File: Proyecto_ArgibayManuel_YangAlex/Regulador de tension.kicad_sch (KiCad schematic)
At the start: 11 parts, among them IC1 LM1117

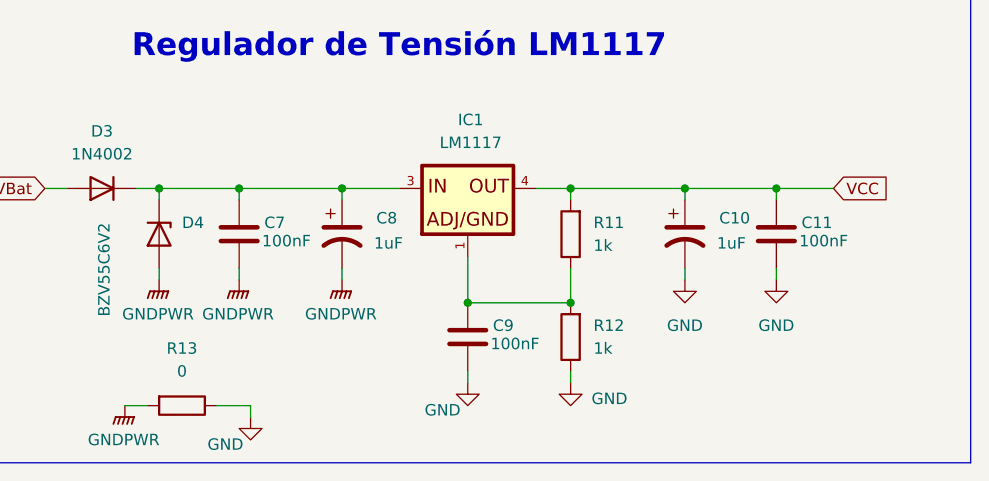
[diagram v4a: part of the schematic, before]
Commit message: Empiezo layout, cambio footprints y arreglo esquematico
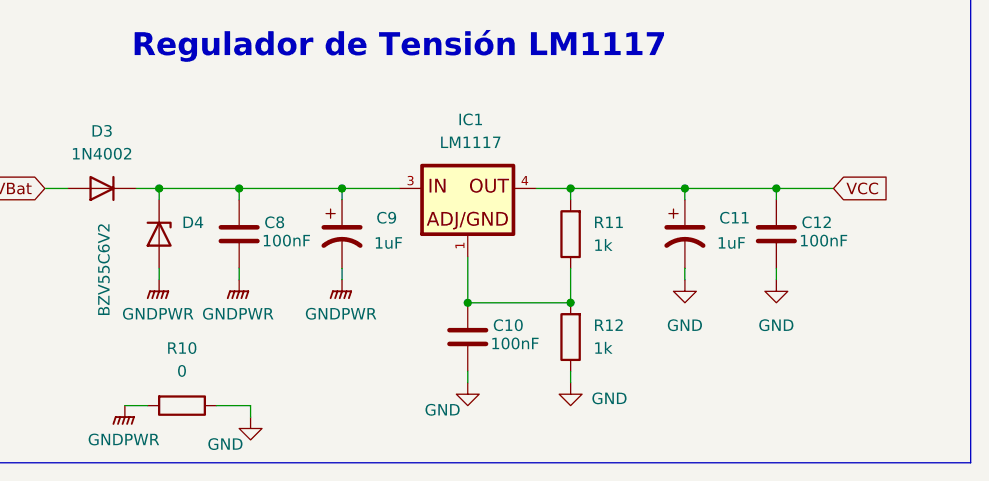
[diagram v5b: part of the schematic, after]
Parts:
- C10: renamed from C9; footprint Capacitor_SMD:C_0805_2012Metric -> Capacitor_THT:CP_Radial_D5.0mm_P2.00mm
- C11: renamed from C10; footprint Capacitor_SMD:C_0805_2012Metric -> Capacitor_THT:CP_Radial_D5.0mm_P2.00mm
- C12: renamed from C11; footprint Capacitor_SMD:C_0805_2012Metric -> Capacitor_THT:CP_Radial_D5.0mm_P2.00mm
- C8: renamed from C7; footprint Capacitor_SMD:C_0805_2012Metric -> Capacitor_THT:CP_Radial_D5.0mm_P2.00mm
- C9: renamed from C8; footprint Capacitor_SMD:C_0805_2012Metric -> Capacitor_THT:CP_Radial_D5.0mm_P2.00mm
- IC1: footprint LM1117:SOT223 -> Footprints:LM1117
- R10: renamed from R13; footprint Resistor_THT:R_Axial_DIN0204_L3.6mm_D1.6mm_P1.90mm_Vertical -> Resistor_SMD:R_0805_2012Metric
- R11, R12: footprint Resistor_THT:R_Axial_DIN0204_L3.6mm_D1.6mm_P1.90mm_Vertical -> Resistor_SMD:R_0805_2012Metric
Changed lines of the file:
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@@
 		(on_board yes)
 		(dnp no)
-		(property "Reference" "#PWR039"
+		(property "Reference" "#PWR027"
 			(at 138.43 106.68 0)
 			(effects
@@
 			(project "Proyecto_ArgibayManuel_YangAlex"
 				(path "/b2dde924-33f5-41ab-a1bf-811873450a89/586cebd2-39d7-435a-989d-0b17f5522a13"
-					(reference "#PWR039")
+					(reference "#PWR027")
 					(unit 1)
 				)
@@
 		(dnp no)
 		(fields_autoplaced yes)
-		(property "Reference" "#PWR025"
+		(property "Reference" "#PWR026"
 			(at 137.16 90.17 0)
 			(effects
@@
 			(project "Proyecto_ArgibayManuel_YangAlex"
 				(path "/b2dde924-33f5-41ab-a1bf-811873450a89/586cebd2-39d7-435a-989d-0b17f5522a13"
-					(reference "#PWR025")
+					(reference "#PWR026")
 					(unit 1)
 				)
@@
 		(dnp no)
 		(fields_autoplaced yes)
-		(property "Reference" "#PWR029"
+		(property "Reference" "#PWR031"
 			(at 186.69 91.44 0)
 			(effects
@@
 			(project "Proyecto_ArgibayManuel_YangAlex"
 				(path "/b2dde924-33f5-41ab-a1bf-811873450a89/586cebd2-39d7-435a-989d-0b17f5522a13"
-					(reference "#PWR029")
+					(reference "#PWR031")
 					(unit 1)
 				)
@@
 			)
 		)
-		(property "Footprint" "LM1117:SOT223"
+		(property "Footprint" "Footprints:LM1117"
 			(at 162.56 74.93 0)
 			(effects
@@
 		(on_board yes)
 		(dnp no)
-		(property "Reference" "C7"
+		(property "Reference" "C8"
 			(at 139.954 78.74 0)
 			(effects
@@
 			)
 		)
-		(property "Footprint" "Capacitor_SMD:C_0805_2012Metric"
+		(property "Footprint" "Capacitor_THT:CP_Radial_D5.0mm_P2.00mm"
 			(at 138.1252 83.82 0)
 			(effects
@@
 			(project "Proyecto_ArgibayManuel_YangAlex"
 				(path "/b2dde924-33f5-41ab-a1bf-811873450a89/586cebd2-39d7-435a-989d-0b17f5522a13"
-					(reference "C7")
+					(reference "C8")
 					(unit 1)
 				)
@@
 		(on_board yes)
 		(dnp no)
-		(property "Reference" "#PWR028"
+		(property "Reference" "#PWR030"
 			(at 173.99 102.87 0)
 			(effects
@@
 			(project "Proyecto_ArgibayManuel_YangAlex"
 				(path "/b2dde924-33f5-41ab-a1bf-811873450a89/586cebd2-39d7-435a-989d-0b17f5522a13"
-					(reference "#PWR028")
+					(reference "#PWR030")
 					(unit 1)
 				)
@@
 		(dnp no)
 		(fields_autoplaced yes)
-		(property "Reference" "R13"
+		(property "Reference" "R10"
 			(at 130.81 92.71 90)
 			(effects
@@
 			)
 		)
-		(property "Footprint" "Resistor_THT:R_Axial_DIN0204_L3.6mm_D1.6mm_P1.90mm_Vertical"
+		(property "Footprint" "Resistor_SMD:R_0805_2012Metric"
 			(at 130.81 97.282 90)
 			(effects
@@
 			(project "Proyecto_ArgibayManuel_YangAlex"
 				(path "/b2dde924-33f5-41ab-a1bf-811873450a89/586cebd2-39d7-435a-989d-0b17f5522a13"
-					(reference "R13")
+					(reference "R10")
 					(unit 1)
 				)
@@
 		(on_board yes)
 		(dnp no)
-		(property "Reference" "C8"
+		(property "Reference" "C9"
 			(at 152.4 78.232 0)
 			(effects
@@
 			)
 		)
-		(property "Footprint" "Capacitor_SMD:C_0805_2012Metric"
+		(property "Footprint" "Capacitor_THT:CP_Radial_D5.0mm_P2.00mm"
 			(at 148.59 80.01 0)
 			(effects
@@
 			(project "Proyecto_ArgibayManuel_YangAlex"
 				(path "/b2dde924-33f5-41ab-a1bf-811873450a89/586cebd2-39d7-435a-989d-0b17f5522a13"
-					(reference "C8")
+					(reference "C9")
 					(unit 1)
 				)
@@
 		(dnp no)
 		(fields_autoplaced yes)
-		(property "Reference" "#PWR024"
+		(property "Reference" "#PWR025"
 			(at 128.27 90.17 0)
 			(effects
@@
 			(project "Proyecto_ArgibayManuel_YangAlex"
 				(path "/b2dde924-33f5-41ab-a1bf-811873450a89/586cebd2-39d7-435a-989d-0b17f5522a13"
-					(reference "#PWR024")
+					(reference "#PWR025")
 					(unit 1)
 				)
@@
 		(dnp no)
 		(fields_autoplaced yes)
-		(property "Reference" "#PWR030"
+		(property "Reference" "#PWR032"
 			(at 196.85 91.44 0)
 			(effects
@@
 			(project "Proyecto_ArgibayManuel_YangAlex"
 				(path "/b2dde924-33f5-41ab-a1bf-811873450a89/586cebd2-39d7-435a-989d-0b17f5522a13"
-					(reference "#PWR030")
+					(reference "#PWR032")
 					(unit 1)
 				)
@@
 			)
 		)
-		(property "Footprint" "Resistor_THT:R_Axial_DIN0204_L3.6mm_D1.6mm_P1.90mm_Vertical"
+		(property "Footprint" "Resistor_SMD:R_0805_2012Metric"
 			(at 175.768 80.01 90)
 			(effects
@@
 		(dnp no)
 		(fields_autoplaced yes)
-		(property "Reference" "#PWR026"
+		(property "Reference" "#PWR028"
 			(at 148.59 90.17 0)
 			(effects
@@
 			(project "Proyecto_ArgibayManuel_YangAlex"
 				(path "/b2dde924-33f5-41ab-a1bf-811873450a89/586cebd2-39d7-435a-989d-0b17f5522a13"
-					(reference "#PWR026")
+					(reference "#PWR028")
 					(unit 1)
 				)
@@
 			)
 		)
-		(property "Footprint" "Resistor_THT:R_Axial_DIN0204_L3.6mm_D1.6mm_P1.90mm_Vertical"
+		(property "Footprint" "Resistor_SMD:R_0805_2012Metric"
 			(at 175.768 91.44 90)
 			(effects
@@
 		(on_board yes)
 		(dnp no)
-		(property "Reference" "C9"
+		(property "Reference" "C10"
 			(at 165.354 90.17 0)
 			(effects
@@
 			)
 		)
-		(property "Footprint" "Capacitor_SMD:C_0805_2012Metric"
+		(property "Footprint" "Capacitor_THT:CP_Radial_D5.0mm_P2.00mm"
 			(at 163.5252 95.25 0)
 			(effects
@@
 			(project "Proyecto_ArgibayManuel_YangAlex"
 				(path "/b2dde924-33f5-41ab-a1bf-811873450a89/586cebd2-39d7-435a-989d-0b17f5522a13"
-					(reference "C9")
+					(reference "C10")
 					(unit 1)
 				)
@@
 		(dnp no)
 		(fields_autoplaced yes)
-		(property "Reference" "#PWR038"
+		(property "Reference" "#PWR024"
 			(at 124.46 104.14 0)
 			(effects
@@
 			(project "Proyecto_ArgibayManuel_YangAlex"
 				(path "/b2dde924-33f5-41ab-a1bf-811873450a89/586cebd2-39d7-435a-989d-0b17f5522a13"
-					(reference "#PWR038")
+					(reference "#PWR024")
 					(unit 1)
 				)
@@
 		(on_board yes)
 		(dnp no)
-		(property "Reference" "#PWR027"
+		(property "Reference" "#PWR029"
 			(at 162.56 102.87 0)
 			(effects
@@
 			(project "Proyecto_ArgibayManuel_YangAlex"
 				(path "/b2dde924-33f5-41ab-a1bf-811873450a89/586cebd2-39d7-435a-989d-0b17f5522a13"
-					(reference "#PWR027")
+					(reference "#PWR029")
 					(unit 1)
 				)
@@
 		(on_board yes)
 		(dnp no)
-		(property "Reference" "C11"
+		(property "Reference" "C12"
 			(at 199.644 78.74 0)
 			(effects
@@
 			)
 		)
-		(property "Footprint" "Capacitor_SMD:C_0805_2012Metric"
+		(property "Footprint" "Capacitor_THT:CP_Radial_D5.0mm_P2.00mm"
 			(at 197.8152 83.82 0)
 			(effects
@@
 			(project "Proyecto_ArgibayManuel_YangAlex"
 				(path "/b2dde924-33f5-41ab-a1bf-811873450a89/586cebd2-39d7-435a-989d-0b17f5522a13"
-					(reference "C11")
+					(reference "C12")
 					(unit 1)
 				)
@@
 		(on_board yes)
 		(dnp no)
-		(property "Reference" "C10"
+		(property "Reference" "C11"
 			(at 190.5 78.232 0)
 			(effects
@@
 			)
 		)
-		(property "Footprint" "Capacitor_SMD:C_0805_2012Metric"
+		(property "Footprint" "Capacitor_THT:CP_Radial_D5.0mm_P2.00mm"
 			(at 186.69 80.01 0)
 			(effects
@@
 			(project "Proyecto_ArgibayManuel_YangAlex"
 				(path "/b2dde924-33f5-41ab-a1bf-811873450a89/586cebd2-39d7-435a-989d-0b17f5522a13"
-					(reference "C10")
-					(unit 1)
-				)
+					(reference "C11")
+					(unit 1)
+				)

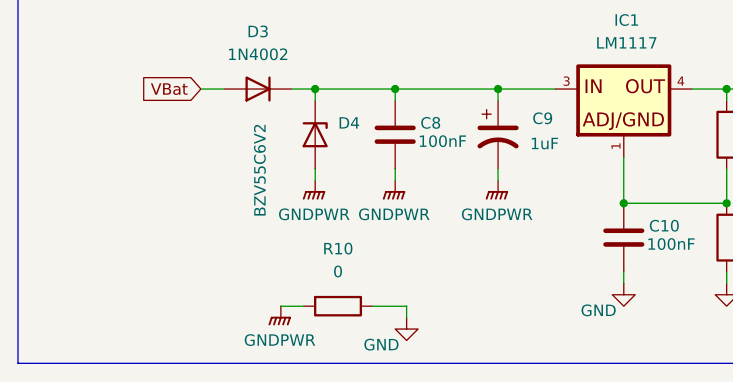
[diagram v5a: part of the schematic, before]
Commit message: Cambio de presentacion(esquematico,consumo,layout), minimas correciones en el esquematico
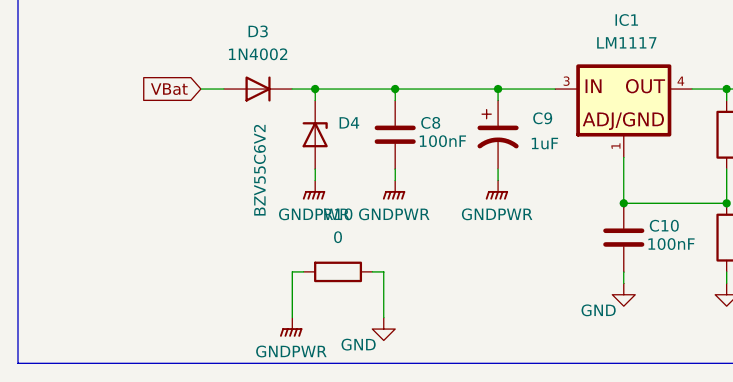
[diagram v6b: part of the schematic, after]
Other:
- moved on the sheet: R10
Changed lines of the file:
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@@
 	(wire
 		(pts
-			(xy 134.62 99.06) (xy 138.43 99.06)
+			(xy 134.62 95.25) (xy 135.89 95.25)
 		)
 		(stroke
@@
 	(wire
 		(pts
-			(xy 138.43 99.06) (xy 138.43 100.33)
+			(xy 135.89 95.25) (xy 135.89 100.33)
 		)
 		(stroke
@@
 	(wire
 		(pts
-			(xy 124.46 99.06) (xy 127 99.06)
+			(xy 125.73 95.25) (xy 127 95.25)
 		)
 		(stroke
@@
 		(pts
 			(xy 137.16 74.93) (xy 137.16 76.2)
+		)
+		(stroke
+			(width 0)
+			(type default)
+		)
+	)
+	(wire
+		(pts
+			(xy 125.73 95.25) (xy 125.73 100.33)
 		)
 		(stroke
@@
 	(symbol
 		(lib_id "power:GND")
-		(at 138.43 100.33 0)
-		(unit 1)
-		(exclude_from_sim no)
-		(in_bom yes)
-		(on_board yes)
-		(dnp no)
-		(property "Reference" "#PWR027"
-			(at 138.43 106.68 0)
+		(at 135.89 100.33 0)
+		(unit 1)
+		(exclude_from_sim no)
+		(in_bom yes)
+		(on_board yes)
+		(dnp no)
+		(property "Reference" "#PWR028"
+			(at 135.89 106.68 0)
 			(effects
 				(font
@@
 		)
 		(property "Value" "GND"
-			(at 135.636 103.378 0)
+			(at 133.096 103.378 0)
 			(effects
 				(font
@@
 		)
 		(property "Footprint" ""
-			(at 138.43 100.33 0)
+			(at 135.89 100.33 0)
 			(effects
 				(font
@@
 		)
 		(property "Datasheet" ""
-			(at 138.43 100.33 0)
+			(at 135.89 100.33 0)
 			(effects
 				(font
@@
 		)
 		(property "Description" "Power symbol creates a global label with name \"GND\" , ground"
-			(at 138.43 100.33 0)
-			(effects
-				(font
-					(size 1.27 1.27)
-				)
-				(hide yes)
-			)
-		)
-		(pin "1"
-		)
-		(instances
-			(project "Proyecto_ArgibayManuel_YangAlex"
-				(path "/b2dde924-33f5-41ab-a1bf-811873450a89/586cebd2-39d7-435a-989d-0b17f5522a13"
-					(reference "#PWR027")
+			(at 135.89 100.33 0)
+			(effects
+				(font
+					(size 1.27 1.27)
+				)
+				(hide yes)
+			)
+		)
+		(pin "1"
+		)
+		(instances
+			(project "Proyecto_ArgibayManuel_YangAlex"
+				(path "/b2dde924-33f5-41ab-a1bf-811873450a89/586cebd2-39d7-435a-989d-0b17f5522a13"
+					(reference "#PWR028")
 					(unit 1)
 				)
@@
 		(dnp no)
 		(fields_autoplaced yes)
-		(property "Reference" "#PWR026"
+		(property "Reference" "#PWR027"
 			(at 137.16 90.17 0)
 			(effects
@@
 			(project "Proyecto_ArgibayManuel_YangAlex"
 				(path "/b2dde924-33f5-41ab-a1bf-811873450a89/586cebd2-39d7-435a-989d-0b17f5522a13"
-					(reference "#PWR026")
+					(reference "#PWR027")
 					(unit 1)
 				)
@@
 		(dnp no)
 		(fields_autoplaced yes)
-		(property "Reference" "#PWR031"
+		(property "Reference" "#PWR032"
 			(at 186.69 91.44 0)
 			(effects
@@
 			(project "Proyecto_ArgibayManuel_YangAlex"
 				(path "/b2dde924-33f5-41ab-a1bf-811873450a89/586cebd2-39d7-435a-989d-0b17f5522a13"
-					(reference "#PWR031")
+					(reference "#PWR032")
 					(unit 1)
 				)
@@
 		(on_board yes)
 		(dnp no)
-		(property "Reference" "#PWR030"
+		(property "Reference" "#PWR031"
 			(at 173.99 102.87 0)
 			(effects
@@
 			(project "Proyecto_ArgibayManuel_YangAlex"
 				(path "/b2dde924-33f5-41ab-a1bf-811873450a89/586cebd2-39d7-435a-989d-0b17f5522a13"
-					(reference "#PWR030")
+					(reference "#PWR031")
 					(unit 1)
 				)
@@
 	(symbol
 		(lib_id "Device:R")
-		(at 130.81 99.06 270)
+		(at 130.81 95.25 270)
 		(unit 1)
 		(exclude_from_sim no)
@@
 		(fields_autoplaced yes)
 		(property "Reference" "R10"
-			(at 130.81 92.71 90)
+			(at 130.81 88.9 90)
 			(effects
 				(font
@@
 		)
 		(property "Value" "0"
-			(at 130.81 95.25 90)
+			(at 130.81 91.44 90)
 			(effects
 				(font
@@
 		)
 		(property "Footprint" "Resistor_SMD:R_0805_2012Metric"
-			(at 130.81 97.282 90)
+			(at 130.81 93.472 90)
 			(effects
 				(font
@@
 		)
 		(property "Datasheet" "~"
-			(at 130.81 99.06 0)
+			(at 130.81 95.25 0)
 			(effects
 				(font
@@
 		)
 		(property "Description" "Resistor"
-			(at 130.81 99.06 0)
+			(at 130.81 95.25 0)
 			(effects
 				(font
@@
 		(dnp no)
 		(fields_autoplaced yes)
-		(property "Reference" "#PWR025"
+		(property "Reference" "#PWR026"
 			(at 128.27 90.17 0)
 			(effects
@@
 			(project "Proyecto_ArgibayManuel_YangAlex"
 				(path "/b2dde924-33f5-41ab-a1bf-811873450a89/586cebd2-39d7-435a-989d-0b17f5522a13"
-					(reference "#PWR025")
+					(reference "#PWR026")
 					(unit 1)
 				)
@@
 		(dnp no)
 		(fields_autoplaced yes)
-		(property "Reference" "#PWR032"
+		(property "Reference" "#PWR033"
 			(at 196.85 91.44 0)
 			(effects
@@
 			(project "Proyecto_ArgibayManuel_YangAlex"
 				(path "/b2dde924-33f5-41ab-a1bf-811873450a89/586cebd2-39d7-435a-989d-0b17f5522a13"
-					(reference "#PWR032")
+					(reference "#PWR033")
 					(unit 1)
 				)
@@
 		(dnp no)
 		(fields_autoplaced yes)
-		(property "Reference" "#PWR028"
+		(property "Reference" "#PWR029"
 			(at 148.59 90.17 0)
 			(effects
@@
 			(project "Proyecto_ArgibayManuel_YangAlex"
 				(path "/b2dde924-33f5-41ab-a1bf-811873450a89/586cebd2-39d7-435a-989d-0b17f5522a13"
-					(reference "#PWR028")
+					(reference "#PWR029")
 					(unit 1)
 				)
@@
 	(symbol
 		(lib_id "power:GNDPWR")
-		(at 124.46 99.06 0)
+		(at 125.73 100.33 0)
 		(unit 1)
 		(exclude_from_sim no)
@@
 		(dnp no)
 		(fields_autoplaced yes)
-		(property "Reference" "#PWR024"
-			(at 124.46 104.14 0)
+		(property "Reference" "#PWR025"
+			(at 125.73 105.41 0)
 			(effects
 				(font
@@
 		)
 		(property "Value" "GNDPWR"
-			(at 124.333 102.87 0)
+			(at 125.603 104.14 0)
 			(effects
 				(font
@@
 		)
 		(property "Footprint" ""
-			(at 124.46 100.33 0)
+			(at 125.73 101.6 0)
 			(effects
 				(font
@@
 		)
 		(property "Datasheet" ""
-			(at 124.46 100.33 0)
+			(at 125.73 101.6 0)
 			(effects
 				(font
@@
 		)
 		(property "Description" "Power symbol creates a global label with name \"GNDPWR\" , global ground"
-			(at 124.46 99.06 0)
-			(effects
-				(font
-					(size 1.27 1.27)
-				)
-				(hide yes)
-			)
-		)
-		(pin "1"
-		)
-		(instances
-			(project "Proyecto_ArgibayManuel_YangAlex"
-				(path "/b2dde924-33f5-41ab-a1bf-811873450a89/586cebd2-39d7-435a-989d-0b17f5522a13"
-					(reference "#PWR024")
+			(at 125.73 100.33 0)
+			(effects
+				(font
+					(size 1.27 1.27)
+				)
+				(hide yes)
+			)
+		)
+		(pin "1"
+		)
+		(instances
+			(project "Proyecto_ArgibayManuel_YangAlex"
+				(path "/b2dde924-33f5-41ab-a1bf-811873450a89/586cebd2-39d7-435a-989d-0b17f5522a13"
+					(reference "#PWR025")
 					(unit 1)
 				)
@@
 		(on_board yes)
 		(dnp no)
-		(property "Reference" "#PWR029"
+		(property "Reference" "#PWR030"
 			(at 162.56 102.87 0)
 			(effects
@@
 			(project "Proyecto_ArgibayManuel_YangAlex"
 				(path "/b2dde924-33f5-41ab-a1bf-811873450a89/586cebd2-39d7-435a-989d-0b17f5522a13"
-					(reference "#PWR029")
-					(unit 1)
-				)
+					(reference "#PWR030")
+					(unit 1)
+				)

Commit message: Arreglo errores y cambio conector
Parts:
- R10: footprint Resistor_SMD:R_0805_2012Metric -> Resistor_THT:R_Axial_DIN0204_L3.6mm_D1.6mm_P5.08mm_Vertical
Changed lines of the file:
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@@
 			)
 		)
-		(property "Footprint" "Resistor_SMD:R_0805_2012Metric"
+		(property "Footprint" "Resistor_THT:R_Axial_DIN0204_L3.6mm_D1.6mm_P5.08mm_Vertical"
 			(at 130.81 93.472 90)
 			(effects

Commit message: Arreglo layout y esqumatico con las correcciones pasadas
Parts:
- C10, C11, C12, C8, C9: footprint Capacitor_THT:CP_Radial_D5.0mm_P2.00mm -> Capacitor_SMD:C_0805_2012Metric
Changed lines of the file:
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@@
 			)
 		)
-		(property "Footprint" "Capacitor_THT:CP_Radial_D5.0mm_P2.00mm"
+		(property "Footprint" "Capacitor_SMD:C_0805_2012Metric"
 			(at 138.1252 83.82 0)
 			(effects
@@
 			)
 		)
-		(property "Footprint" "Capacitor_THT:CP_Radial_D5.0mm_P2.00mm"
+		(property "Footprint" "Capacitor_SMD:C_0805_2012Metric"
 			(at 148.59 80.01 0)
 			(effects
@@
 			)
 		)
-		(property "Footprint" "Capacitor_THT:CP_Radial_D5.0mm_P2.00mm"
+		(property "Footprint" "Capacitor_SMD:C_0805_2012Metric"
 			(at 163.5252 95.25 0)
 			(effects
@@
 			)
 		)
-		(property "Footprint" "Capacitor_THT:CP_Radial_D5.0mm_P2.00mm"
+		(property "Footprint" "Capacitor_SMD:C_0805_2012Metric"
 			(at 197.8152 83.82 0)
 			(effects
@@
 			)
 		)
-		(property "Footprint" "Capacitor_THT:CP_Radial_D5.0mm_P2.00mm"
+		(property "Footprint" "Capacitor_SMD:C_0805_2012Metric"
 			(at 186.69 80.01 0)
 			(effects
